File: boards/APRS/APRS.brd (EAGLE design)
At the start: 50.8 x 38.1 mm, 15 parts

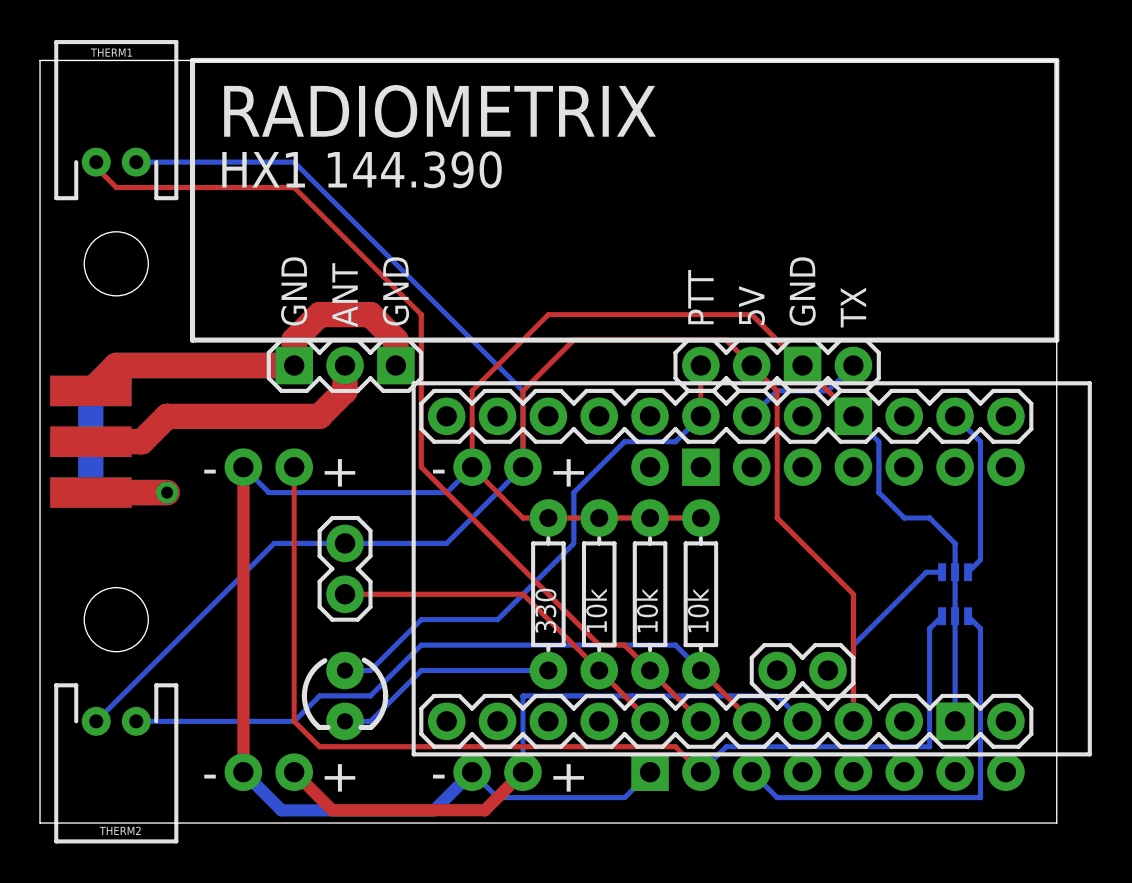
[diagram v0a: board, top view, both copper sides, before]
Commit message: First pass of APRS v2
- Cleaned up the board (removed unnecessary things)
- Switched to using more library objects
- Switched to TPS6300x for power
- Integrated the Venus GPS
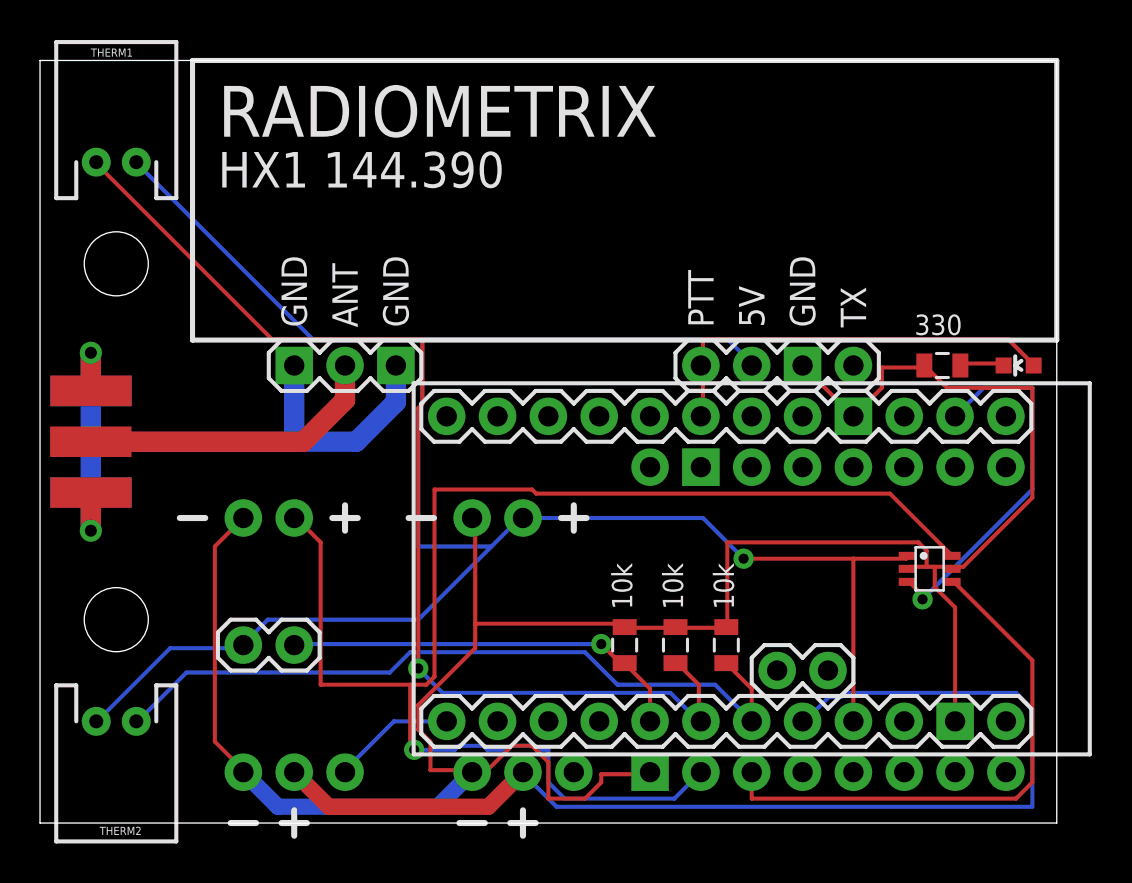
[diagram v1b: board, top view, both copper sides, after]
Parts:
- removed POWER1: 5V, OpenSpace:POWER-TPS6300X
- removed POWER2: 3.3V, OpenSpace:POWER-TPS6300X
- added POWER3: 3.3V, OpenSpace:POWER-TPS6300X
- added POWER5: 5V, OpenSpace:POWER-TPS6300X
- LED1: device SparkFun:LED3MM -> SparkFun-LED:LED-0603
- R1, R_T0, R_T1, R_T2: device SparkFun:AXIAL-0.3 -> SparkFun-Passives:0805
- moved LED1 37.5 mm to (48.9, 22.9), turned to 90 degrees
- moved R1 22.8 mm to (45.1, 22.9), turned to 180 degrees
- moved THERM0 3.59 mm to (12.7, 8.89), turned to 180 degrees
- moved R_T0 2.84 mm to (29.2, 8.89)
- moved R_T1 2.84 mm to (31.8, 8.89)
- moved R_T2 2.84 mm to (34.3, 8.89)
- moved LEVEL_SHIFT 1.80 mm to (44.5, 12.7), flipped to the top, turned to 270 degrees
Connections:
- new net 3.3V_EN: ARDUINO.D10*, POWER3.EN
- net 1.8V: now also POWER3.BATT+, POWER5.BATT+; no longer POWER1.BATT+, POWER2.BATT+
- net 3.3V: now also POWER3.VCC+; no longer POWER2.VCC+
- net 5V: now also POWER5.VCC+; no longer POWER1.VCC+
- net A0: now also R_T0.1; no longer R_T0.P$1
- net A1: now also R_T1.1; no longer R_T1.P$1
- net A2: now also R_T2.1; no longer R_T2.P$1
- net GND: now also POWER3.BATT-, POWER3.VCC-, POWER5.BATT-, POWER5.VCC-, R1.2, R_T0.2, R_T1.2, R_T2.2; no longer POWER1.BATT-, POWER1.VCC-, POWER2.BATT-, POWER2.VCC-, R1.P$2, R_T0.P$2, R_T1.P$2, R_T2.P$2
- net N$11: now also LED1.C, R1.1; no longer LED1.K, R1.P$1
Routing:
- net 1.8V: track 31.3 -> 56.3 mm
- net 3.3V: track 52.8 -> 71.9 mm, vias 0 -> 1
- net GND: track 107.8 -> 119.4 mm
- net RX: track 8.57 -> 18.5 mm, vias 0 -> 1
- net N$11: track 11.2 -> 2.22 mm
- net A1: track 46.4 -> 55.3 mm, vias 0 -> 1
- net N$1: track 42.7 -> 34.4 mm, vias 1 -> 2
- net 3.3V_EN: track 0.00 -> 6.19 mm
- net N$3: track 21.3 -> 27.4 mm
- net D3: track 6.13 -> 0.00 mm
- net D4: track 27.1 -> 21.1 mm
- net A2: track 33.9 -> 37.0 mm
- net A0: track 17.9 -> 20.4 mm, vias 0 -> 1
- net 5V: track 100.9 -> 103.1 mm, vias 0 -> 1

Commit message: New APRS board, close to ready
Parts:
- added I2C_0: (no value), SparkFun-Connectors:1X04
- added I2C_TRANS: PCA9306-D, OpenSpace:SO8
- added SCL_PU, SDA_PU: 3.3k, SparkFun-Passives:0805
- ARDUINO: value ARDUINO_PRO_MINI -> ARDUINO_PRO_MINI-NOSILK; device OpenSpace:ARDUINO_PRO_MINI -> OpenSpace:ARDUINO_PRO_MINI-NOSILK
- GPS0: value VENUS_GPS -> VENUS_GPS-NOSILK; device OpenSpace:VENUS_GPS -> OpenSpace:VENUS_GPS-NOSILK
- POWER3, POWER5: device OpenSpace:POWER-TPS6300X -> OpenSpace:POWER-TPS6300X-NOSILK
- THERM0: value (none) -> 10k; device SparkFun:1X02 -> SparkFun-Passives:0805
- THERM1, THERM2: value (none) -> 10k
- moved THERM0 9.09 mm to (16.5, 17.1), turned to 0 degrees
- moved R_T0 5.85 mm to (30.5, 14.6)
- moved R_T1 5.85 mm to (33.0, 14.6)
- moved R_T2 5.85 mm to (35.6, 14.6)
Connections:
- new net N$4: ARDUINO.A4_SDA, I2C_TRANS.5
- new net N$5: ARDUINO.A5_SCL, I2C_TRANS.6
- new net N$6: ARDUINO.D12, I2C_TRANS.8
- new net SCL: I2C_0.4, I2C_TRANS.3, SDA_PU.1
- new net SDA: I2C_0.3, I2C_TRANS.4, SCL_PU.1
- net 3.3V: now also I2C_0.2, I2C_TRANS.2, SCL_PU.2, SDA_PU.2
- net 5V: now also I2C_TRANS.7, THERM0.1; no longer THERM0.2
- net A0: now also THERM0.2; no longer THERM0.1
- net GND: now also I2C_0.1, I2C_TRANS.1
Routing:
- net 5V: track 103.1 -> 128.3 mm, vias 1 -> 0
- net 1.8V: track 56.3 -> 32.6 mm
- net N$5: track 0.00 -> 17.7 mm
- net N$4: track 0.00 -> 15.2 mm
- net N$3: track 27.4 -> 15.5 mm
- net SCL: track 0.00 -> 10.5 mm
- net N$6: track 0.00 -> 9.97 mm, vias 0 -> 1
- net SDA: track 0.00 -> 9.97 mm
- net RX: track 18.5 -> 12.2 mm
- net GND: track 119.4 -> 113.1 mm, vias 0 -> 1
- net D3: track 0.00 -> 6.13 mm
- net A0: track 20.4 -> 25.0 mm, vias 1 -> 2
- net A1: track 55.3 -> 51.3 mm
- net A2: track 37.0 -> 40.4 mm, vias 0 -> 1
- net 3.3V: track 71.9 -> 75.2 mm
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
